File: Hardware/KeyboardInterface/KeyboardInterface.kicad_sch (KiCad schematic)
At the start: 9 parts, among them J1 PS/2, J2 CIA, J3 POWER, U1 74HC14, U2 74HC595, U3 74HC595

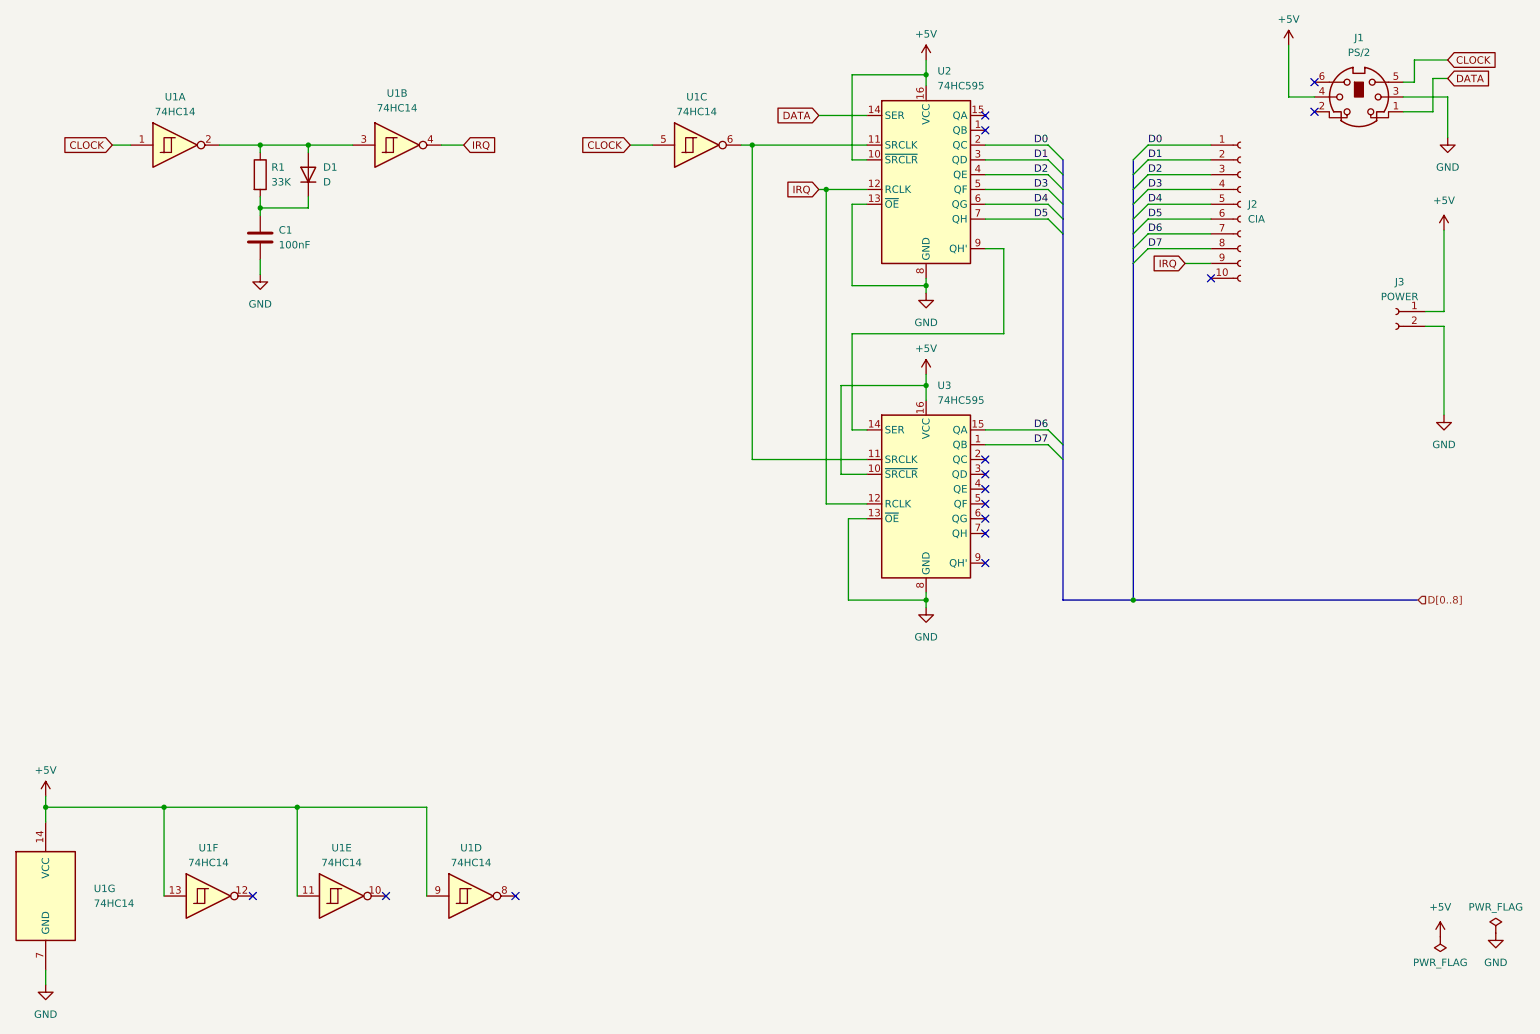
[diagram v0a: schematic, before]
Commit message: Serial Software
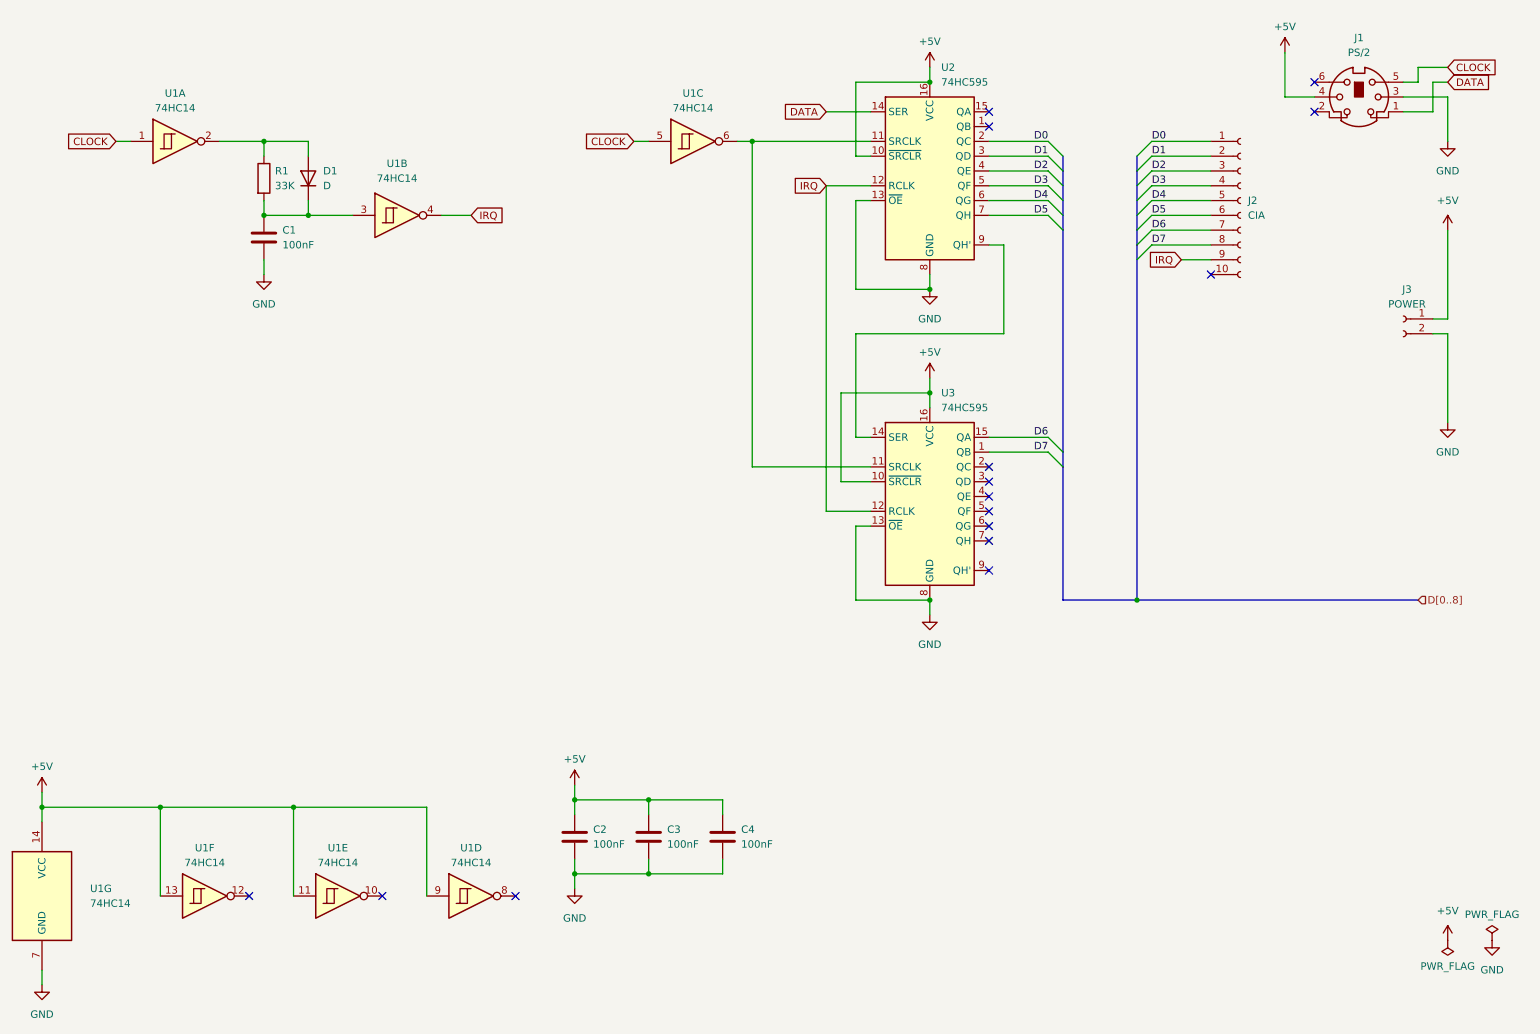
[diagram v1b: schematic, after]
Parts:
- added C2, C3, C4: 100nF, Capacitor_THT:C_Disc_D5.0mm_W2.5mm_P2.50mm, symbol Device:C
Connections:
- net +5V: now also C2.1, C3.1, C4.1
- net GND: now also C2.2, C3.2, C4.2
- net at D1.2 (A), R1.1, U1.2: no longer U1.3
- net at C1.1, D1.1 (K), R1.2: now also U1.3
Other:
- moved on the sheet: C1, D1, J2, J3, R1, U1A, U1B, U1C, U1E, U1F, U1G, U2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
